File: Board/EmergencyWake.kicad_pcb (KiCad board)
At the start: 2 copper layers, 100 x 67 mm, 153 parts, among them J1 USB_C_Receptacle_USB2.0, J10 Conn_01x04, J2 Micro_SD_Card_Det, J3 Conn_01x03, J4 Conn_01x02, J5 Conn_01x05, J6 Conn_01x04, J7 Conn_01x02, J8 Conn_01x04, J9 Conn_01x04, Q1 AO3400A, Q2 AO3401A, Q3 AO3400A, Q4 AO3401A, Q5 AO3401A, SW1 SW_DPDT_x2, SW2 SW_Push, SW3 SW_Push, SW4 SW_Push, U1 M24C02-WMN, U10 L9110S, U11 SRV05-4, U2 AMS1117-3.3, U3 MC34063AD, U4 STM32F407VETx, U5 WM8960, U6 173950378, U7 PT6312B, U8 EL357N-G, U9 EL357N-G, Y1 32,768, Y2 8M

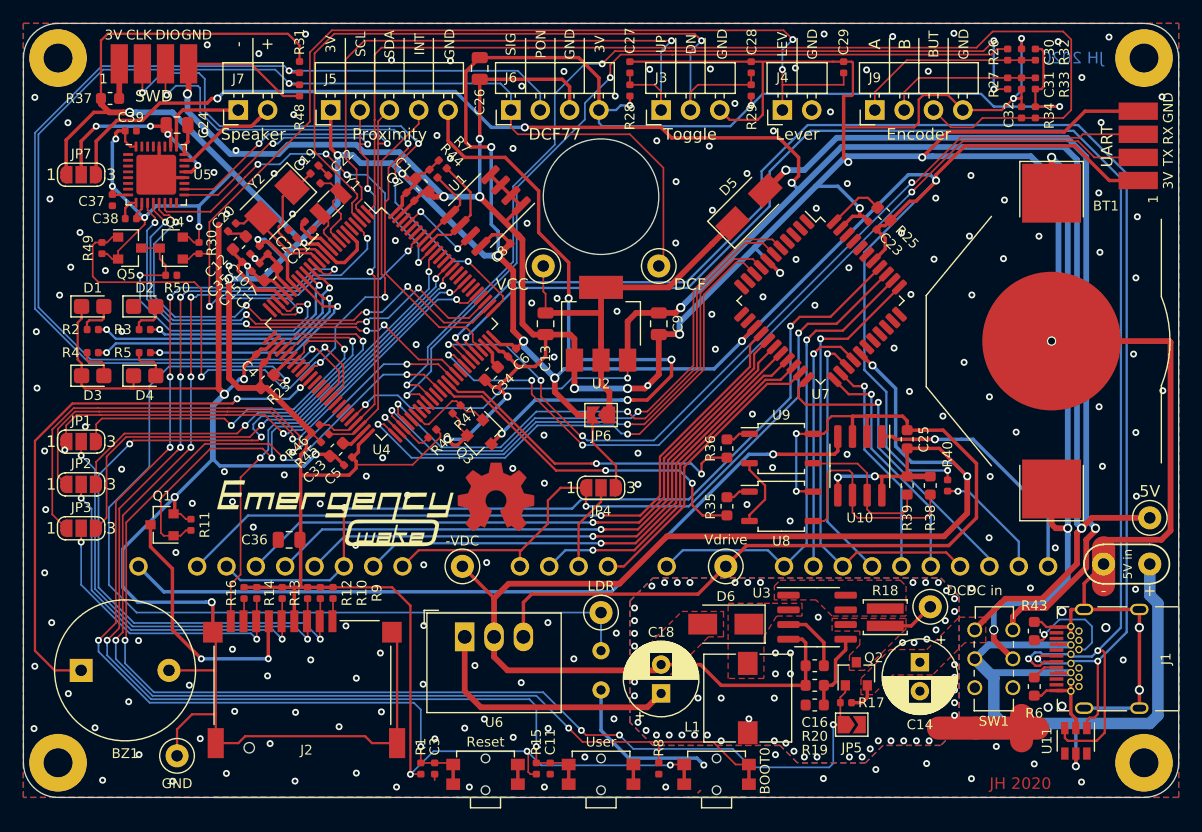
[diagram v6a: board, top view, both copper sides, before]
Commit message: [Board] Minor tweaks, switched position of 5V input and USB protection diodes
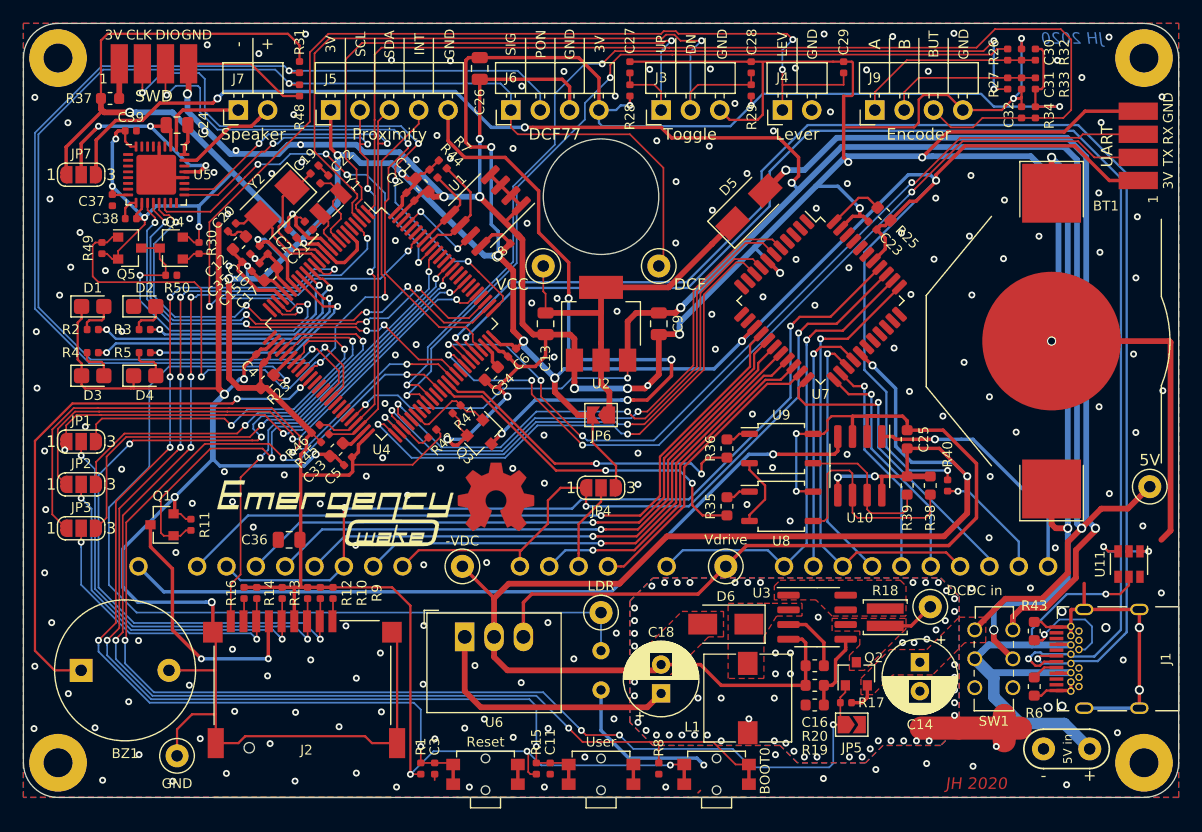
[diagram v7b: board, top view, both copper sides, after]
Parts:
- moved TP1 16.8 mm to (192.3, 162.8)
- moved TP2 16.8 mm to (188.3, 162.8)
- moved U11 16.0 mm to (195.7, 146.8)
- moved TP3 2.70 mm to (197.5, 140.1)
- moved NT1 1.50 mm to (182.9, 161.0)
- moved G*** 0.40 mm to (166.5, 154.0)
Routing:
- net GND: track 547.4 -> 535.6 mm, vias 212 -> 217
- net Net-(J1-PadA4): track 56.2 -> 44.7 mm
- net /USB_DP: track 132.8 -> 123.7 mm
- net /USB_DM: track 128.5 -> 124.7 mm
- net Net-(C24-Pad1): track 18.9 -> 21.0 mm, vias 4 -> 3
- net +5V: track 203.4 -> 204.6 mm

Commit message: [Board] Minor Layout changes
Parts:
- added TP7: MCLK, TestPoint:TestPoint_Loop_D1.80mm_Drill1.0mm_Beaded, F.Cu at (103.2, 119.4)
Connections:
- net /I2C_EN renamed /PROX_EN
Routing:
- net /MCLK: track 38.8 -> 46.3 mm
- net /VFD_DIN: track 48.2 -> 48.8 mm
- net /SD_EN: track 41.6 -> 41.0 mm
- net /VFD_CLK: track 46.8 -> 47.4 mm
- net /VFD_STB: track 47.5 -> 48.1 mm
- net GND: track 535.6 -> 535.1 mm, vias 217 -> 221
- net /SD_CMD: track 42.4 -> 42.6 mm, vias 3 -> 2
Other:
- board text added: "MCLK"
